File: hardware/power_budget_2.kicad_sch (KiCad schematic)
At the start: 0 parts

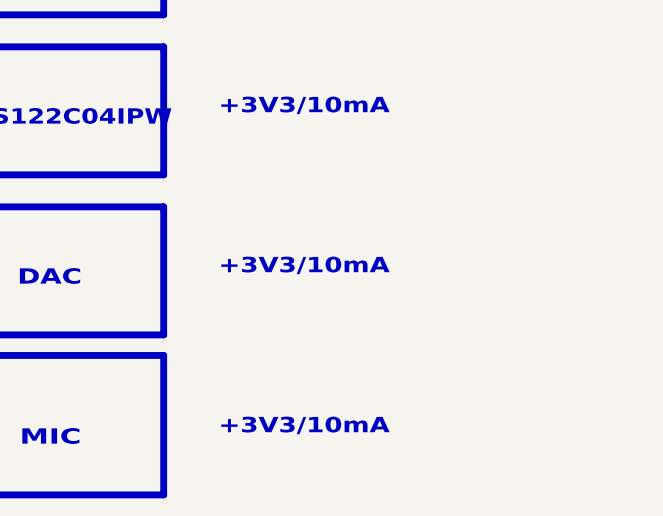
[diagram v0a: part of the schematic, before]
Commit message: Complete Schematic for Power Section
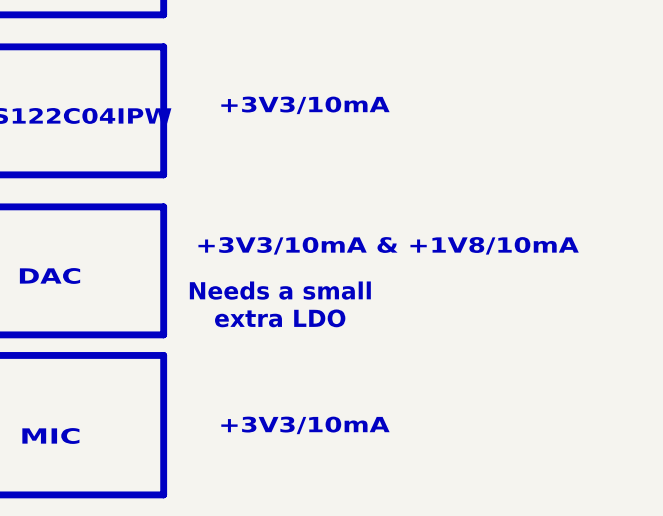
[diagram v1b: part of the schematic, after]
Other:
- note added: "+3V3/10mA & +1V8/10mA"
- note added: "Needs a small extra LDO"
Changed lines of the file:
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@@
+		)
+	)
+	(text "Needs a small\nextra LDO\n"
+		(exclude_from_sim no)
+		(at 231.394 135.636 0)
+		(effects
+			(font
+				(size 1.905 1.905)
+				(thickness 0.381)
+				(bold yes)
+			)
 		)
 	)
@@
 		)
 	)
-	(text "+3V3/10mA"
-		(exclude_from_sim no)
-		(at 224.536 130.1876 0)
-		(effects
-			(font
+	(text "+3V3/10mA & +1V8/10mA\n"
+		(exclude_from_sim no)
+		(at 221.996 128.016 0)
+		(effects
+			(font

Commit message: Organize schematic
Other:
- note added: "+12V 8A Power Input"
- note added: "Needs an extra LDO for +1V8"
- note removed: "+12V Power Input"
- note removed: "Needs a small extra LDO"
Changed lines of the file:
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@@
 		)
 	)
-	(text "Needs a small\nextra LDO\n"
+	(text "Needs an extra\nLDO for +1V8\n"
 		(exclude_from_sim no)
 		(at 231.394 135.636 0)
@@
 	(text "+12V/8A"
 		(exclude_from_sim no)
-		(at 72.39 53.9876 0)
+		(at 70.612 53.086 0)
 		(effects
 			(font
@@
 		)
 	)
-	(text "+12V Power\nInput"
-		(exclude_from_sim no)
-		(at 62.992 42.5576 0)
+	(text "+12V 8A Power\nInput"
+		(exclude_from_sim no)
+		(at 68.834 41.91 0)
 		(effects
 			(font
@@
 				(color 0 0 0 1)
 			)
-			(justify left top)
-		)
-	)
+			(justify top)
+		)
+	)
